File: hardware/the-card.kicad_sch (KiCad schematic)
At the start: 75 parts, among them J1 TYPE-C-31-M-12, J2 FH12-24S-0.5SH(55), J3 S2B-PH-SM4-TB(LF)(SN), Q1 SI2301CDS-T1-GE3, Q2 SI2301CDS-T1-GE3, Q3 Si1304BDL, SW1 TS-1187A-B-A-B, SW2 TS-1187A-B-A-B, SW3 TS-1187A-B-A-B, SW4 TS-1187A-B-A-B, U1 ESP32-S3-WROOM-1-N16R8, U10 USBLC6-2SC6, U2 ST25DV04KC-IE8S3, U3 LSM6DSOTR, U4 SHT40-BD1B-R2, U5 MAX17048G+T10, U6 TP4056_C382139, U7 DW01A_C18164398, U8 FS8205A, U9 ME6211C33M5G-N

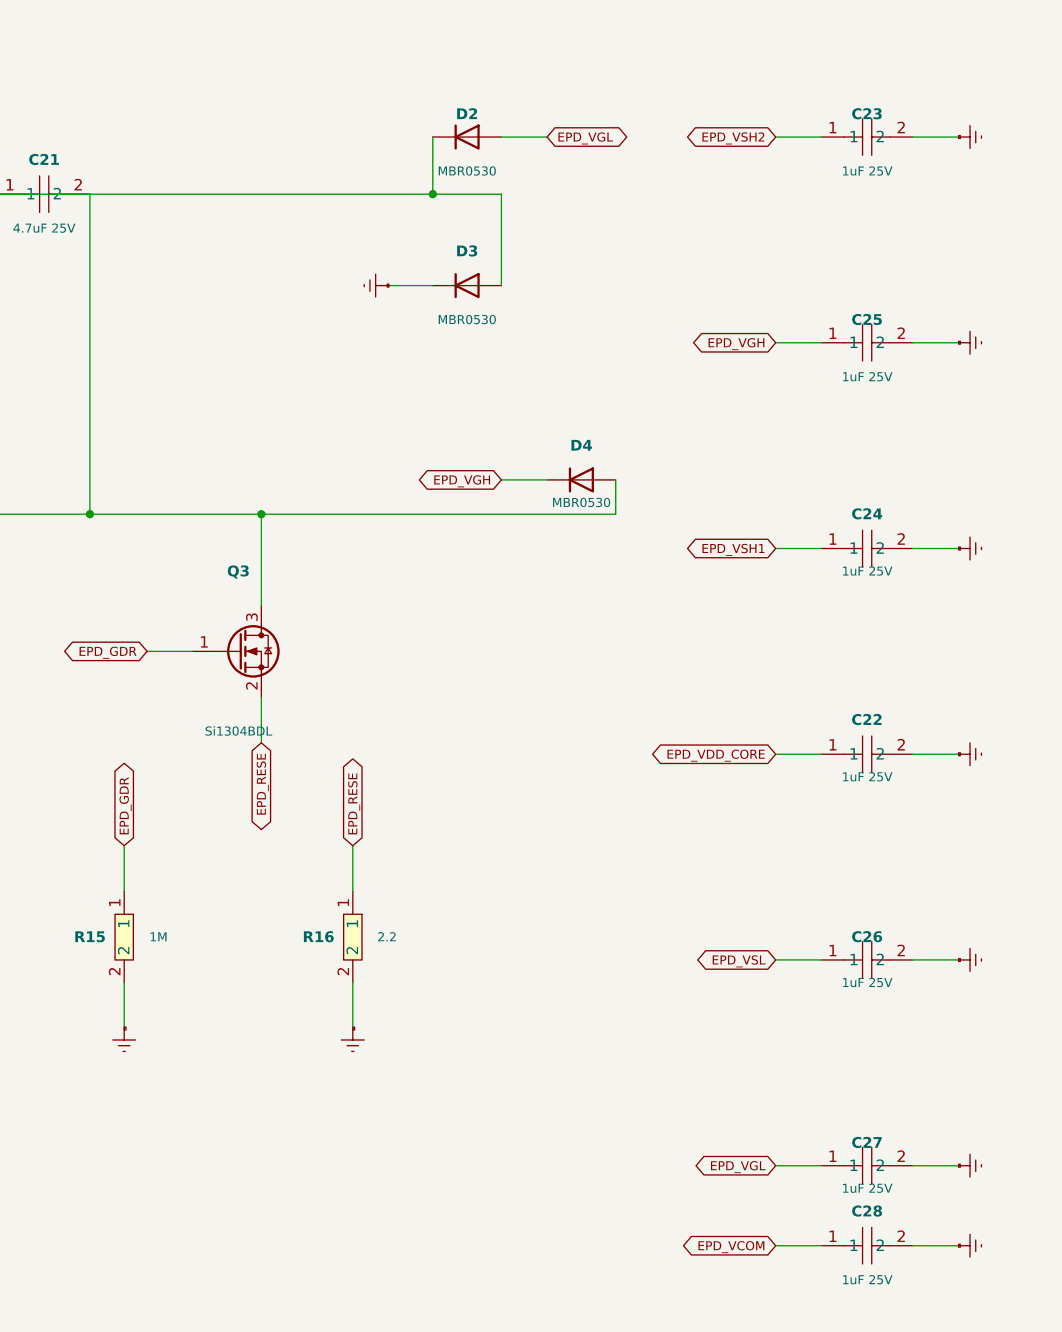
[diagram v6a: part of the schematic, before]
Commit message: fix(hardware): assign fabrication-ready BOM parts
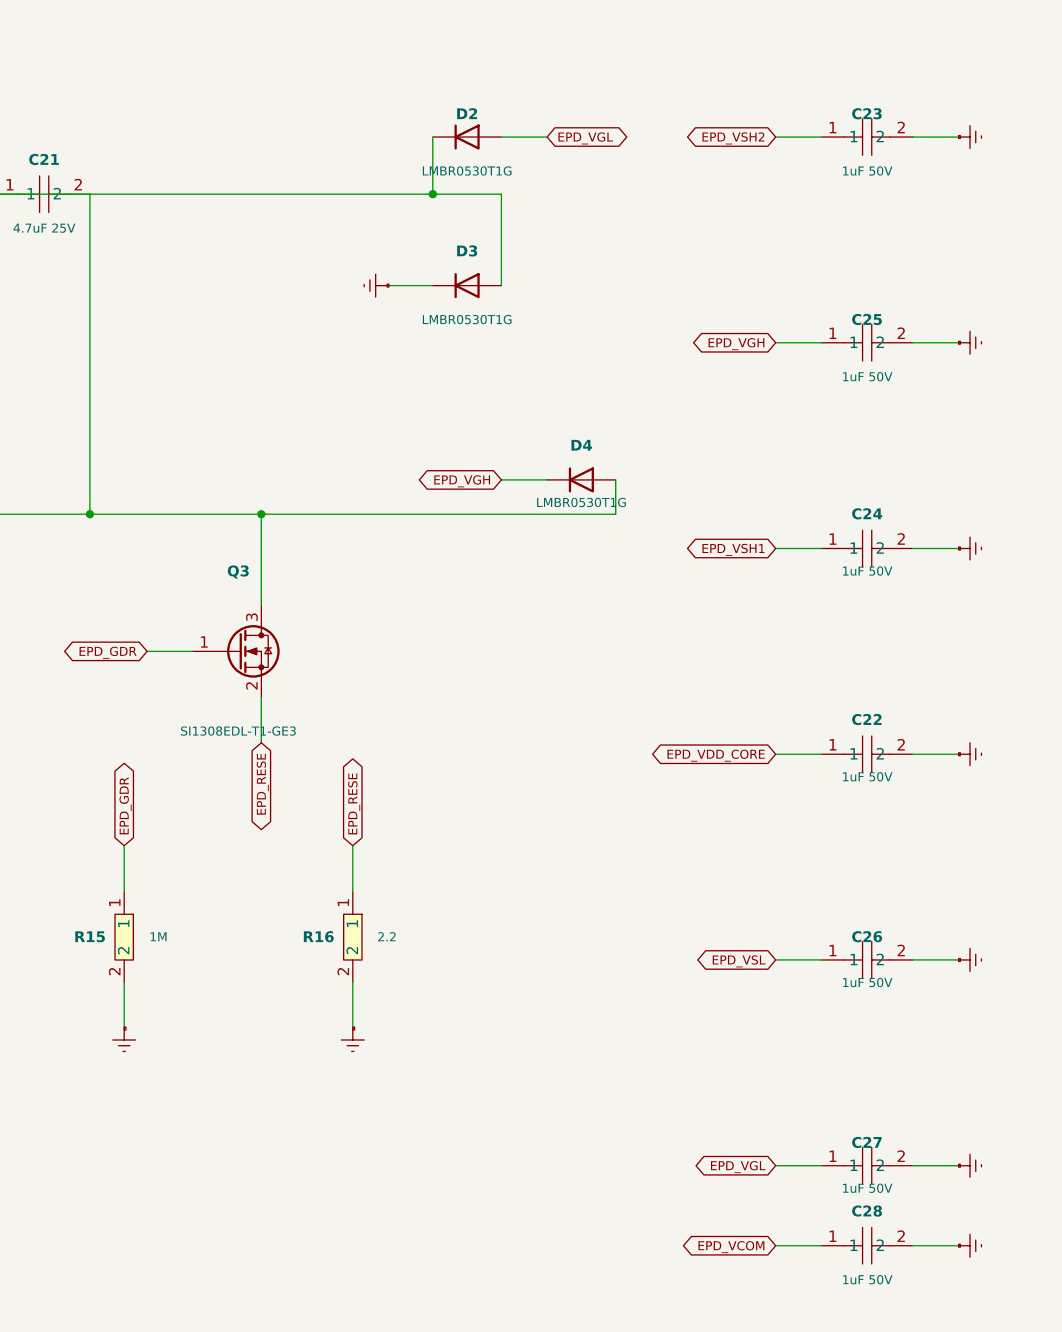
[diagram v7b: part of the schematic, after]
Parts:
- C22, C23, C24, C25, C26, C27, C28: value 1uF 25V -> 1uF 50V
- D2, D3, D4: value MBR0530 -> LMBR0530T1G
- Q3: value Si1304BDL -> SI1308EDL-T1-GE3
- R16: footprint Resistor_SMD:R_0402_1005Metric -> Resistor_SMD:R_1206_3216Metric
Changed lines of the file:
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@@
 			(effects (font (size 1.2 1.2) (bold yes)))
 		)
-		(property "Value" "Si1304BDL"
+		(property "Value" "SI1308EDL-T1-GE3"
 			(at 438.15 307.34 0)
 			(effects (font (size 1 1)))
@@
 			(effects (font (size 1 1)))
 		)
-		(property "Footprint" "Resistor_SMD:R_0402_1005Metric"
+		(property "Footprint" "Resistor_SMD:R_1206_3216Metric"
 			(at 450.85 330.2 0)
 			(effects (font (size 1 1)) (hide yes))
@@
 			(effects (font (size 1.2 1.2) (bold yes)))
 		)
-		(property "Value" "MBR0530"
+		(property "Value" "LMBR0530T1G"
 			(at 463.55 245.11 0)
 			(effects (font (size 1 1)))
@@
 			(effects (font (size 1.2 1.2) (bold yes)))
 		)
-		(property "Value" "MBR0530"
+		(property "Value" "LMBR0530T1G"
 			(at 463.55 261.62 0)
 			(effects (font (size 1 1)))
@@
 			(effects (font (size 1.2 1.2) (bold yes)))
 		)
-		(property "Value" "MBR0530"
+		(property "Value" "LMBR0530T1G"
 			(at 476.25 281.94 0)
 			(effects (font (size 1 1)))
@@
 			(effects (font (size 1.2 1.2) (bold yes)))
 		)
-		(property "Value" "1uF 25V"
+		(property "Value" "1uF 50V"
 			(at 508 312.42 0)
 			(effects (font (size 1 1)))
@@
 			(effects (font (size 1.2 1.2) (bold yes)))
 		)
-		(property "Value" "1uF 25V"
+		(property "Value" "1uF 50V"
 			(at 508 245.11 0)
 			(effects (font (size 1 1)))
@@
 			(effects (font (size 1.2 1.2) (bold yes)))
 		)
-		(property "Value" "1uF 25V"
+		(property "Value" "1uF 50V"
 			(at 508 289.56 0)
 			(effects (font (size 1 1)))
@@
 			(effects (font (size 1.2 1.2) (bold yes)))
 		)
-		(property "Value" "1uF 25V"
+		(property "Value" "1uF 50V"
 			(at 508 267.97 0)
 			(effects (font (size 1 1)))
@@
 			(effects (font (size 1.2 1.2) (bold yes)))
 		)
-		(property "Value" "1uF 25V"
+		(property "Value" "1uF 50V"
 			(at 508 335.28 0)
 			(effects (font (size 1 1)))
@@
 			(effects (font (size 1.2 1.2) (bold yes)))
 		)
-		(property "Value" "1uF 25V"
+		(property "Value" "1uF 50V"
 			(at 508 358.14 0)
 			(effects (font (size 1 1)))
@@
 			(effects (font (size 1.2 1.2) (bold yes)))
 		)
-		(property "Value" "1uF 25V"
+		(property "Value" "1uF 50V"
 			(at 508 368.3 0)
 			(effects (font (size 1 1)))

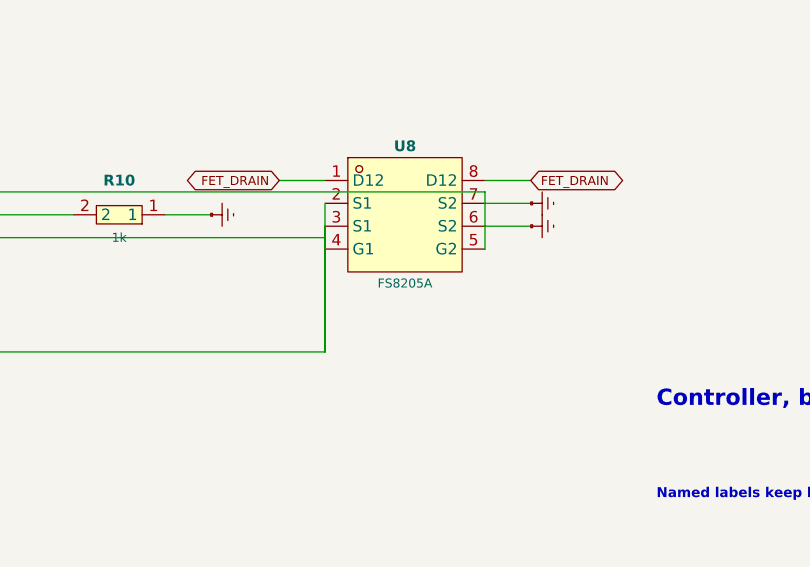
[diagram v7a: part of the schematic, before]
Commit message: fix(hardware): align U8 fabrication metadata
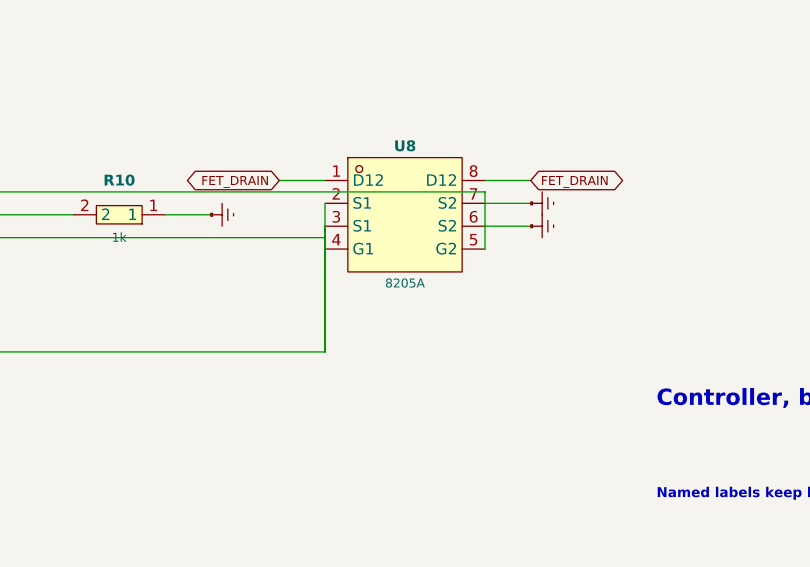
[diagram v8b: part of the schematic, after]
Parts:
- U8: value FS8205A -> 8205A; LCSC Part (none) -> C5148694; MPN (none) -> 8205A; Manufacturer (none) -> HXY MOSFET
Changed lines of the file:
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@@
 			(effects (font (size 1.2 1.2) (bold yes)))
 		)
-		(property "Value" "FS8205A"
+		(property "Value" "8205A"
 			(at 152.4 172.72 0)
 			(effects (font (size 1 1)))
@@
 			(effects (font (size 1 1)) (hide yes))
 		)
-		(property "Datasheet" "https://lcsc.com/product-detail/MOSFET_FS8205A_C16052.html"
+		(property "Datasheet" "https://www.lcsc.com/datasheet/C5148694.pdf"
 			(at 152.4 165.1 0)
 			(effects (font (size 1 1)) (hide yes))
+		)
+		(property "LCSC Part" "C5148694"
+			(at 152.4 165.1 0)
+			(effects (font (size 1 1)) (hide yes))
+		)
+		(property "MPN" "8205A"
+			(at 152.4 165.1 0)
+			(effects (font (size 1 1)) (hide yes))
+		)
+		(property "Manufacturer" "HXY MOSFET"
+			(at 152.4 165.1 0)
+			(effects (font (size 1 1)) (hide yes))
